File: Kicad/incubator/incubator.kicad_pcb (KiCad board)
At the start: 2 copper layers, 99.1 x 73.7 mm, 38 parts, among them J1 Barrel_Jack_MountingPin, J2 Conn_01x06, J4 RJ12, J5 Conn_01x05, SW2 Rotary_Encoder_Switch, U1 AP63205WU, U2 ATmega328P-AU

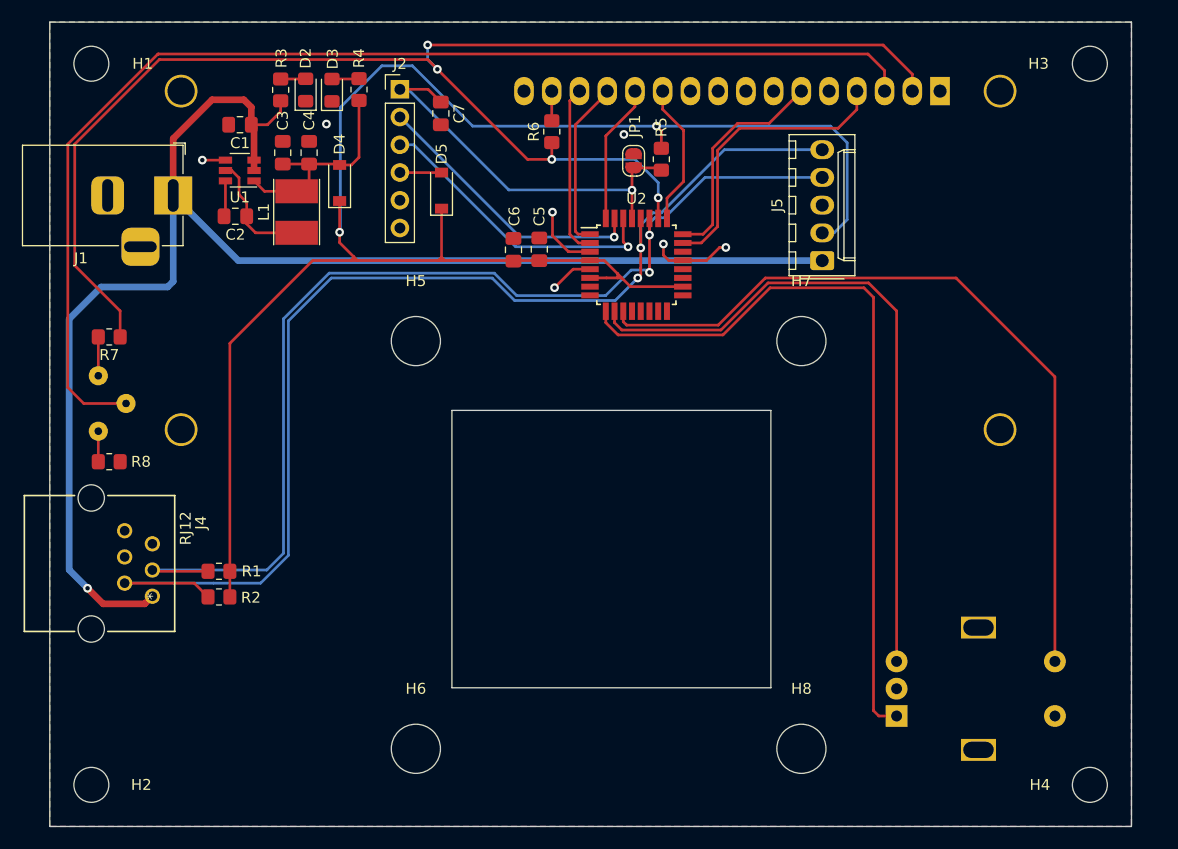
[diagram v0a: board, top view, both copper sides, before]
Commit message: fix: change top-bottom connector for individual pad
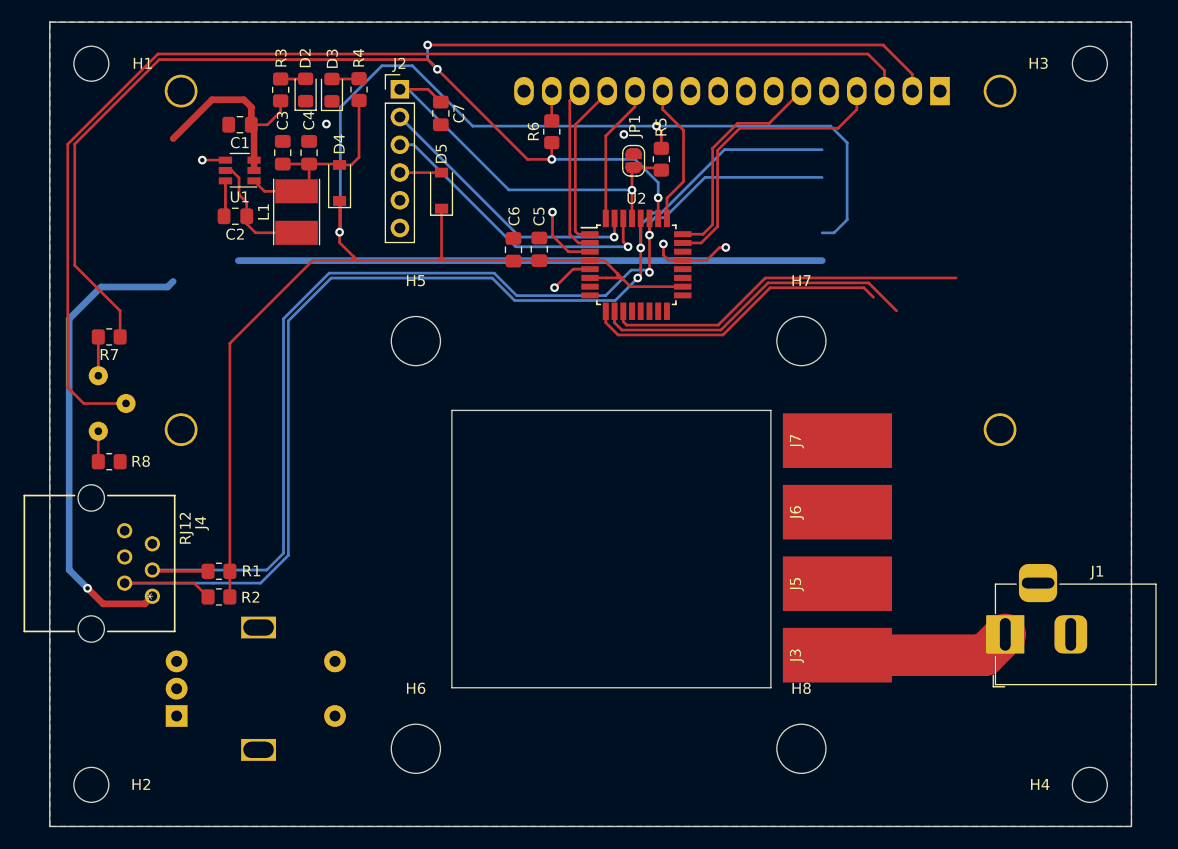
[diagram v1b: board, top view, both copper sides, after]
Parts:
- added J3: Conn_01x01, Connector_Wire:SolderWirePad_1x01_SMD_5x10mm, F.Cu at (72.1, -15.7)
- added J6: Conn_01x01, Connector_Wire:SolderWirePad_1x01_SMD_5x10mm, F.Cu at (72.1, -28.8)
- added J7: Conn_01x01, Connector_Wire:SolderWirePad_1x01_SMD_5x10mm, F.Cu at (72.1, -35.3)
- J5: value Conn_01x05 -> Conn_01x01; footprint Connector_Molex:Molex_KK-254_AE-6410-05A_1x05_P2.54mm_Vertical -> Connector_Wire:SolderWirePad_1x01_SMD_5x10mm
- moved J1 86.2 mm to (87.5, -17.6), turned to 180 degrees
- moved SW2 65.9 mm to (11.6, -10.1)
- moved J5 29.6 mm to (72.1, -22.2)
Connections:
- J5 pad 1: 12V -> GND
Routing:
- net D5: track 68.3 -> 28.2 mm
- net D7: track 72.2 -> 33.4 mm
- net D6: track 62.1 -> 30.0 mm
- net 12V: track 137.1 -> 131.7 mm
